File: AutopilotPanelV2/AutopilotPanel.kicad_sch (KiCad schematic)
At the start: 164 parts, among them J1 USB_C_Receptacle_USB2.0_16P, J10 PINHD_1x2_Male, J2 PINHD_1x2_Male, J3 PINHD_1x2_Male, J4 PINHD_1x2_Male, J5 PINHD_1x2_Male, J6 PINHD_1x2_Male, J7 PINHD_1x2_Male, J8 PINHD_1x2_Male, J9 PINHD_1x2_Male, Q1 NFET-SOT23, Q2 NFET-SOT23, Q3 NFET-SOT23, Q4 NFET-SOT23, Q5 NFET-SOT23, Q6 NFET-SOT23, SW1 SW_SPST_Tactile_6x6, SW10 SW_SPST_Tactile_6x6, SW11 SW_SPST_Tactile_6x6, SW12 SW_SPST_Tactile_6x6, SW13 SW_SPST_Tactile_6x6, SW14 SW_SPST_Tactile_6x6, SW15 RotaryEncoder_Switch_EC11E, SW2 SW_SPST_Tactile_6x6, SW3 SW_SPST_Tactile_6x6, SW4 SW_SPST_Tactile_6x6, SW5 SW_SPST_Tactile_6x6, SW6 SW_SPST_Tactile_6x6, SW7 SW_SPST_Tactile_6x6, SW8 SW_SPST_Tactile_6x6, SW9 SW_SPST_Tactile_6x6, U10 7SegmentFJ5161AH, U11 7SegmentFJ5161AH, U12 7SegmentFJ5161AH, U13 7SegmentFJ5161AH, U14 7SegmentFJ5161AH, U15 74HC165, U16 TPS62160DSG, U17 74HC165, U18 74HC595, U19 74HC595, U20 74HC595, U21 74HC595, U22 74HC595, U23 74HC595, U7 74HC164, U8 74HC164, U9 7SegmentFJ5161AH

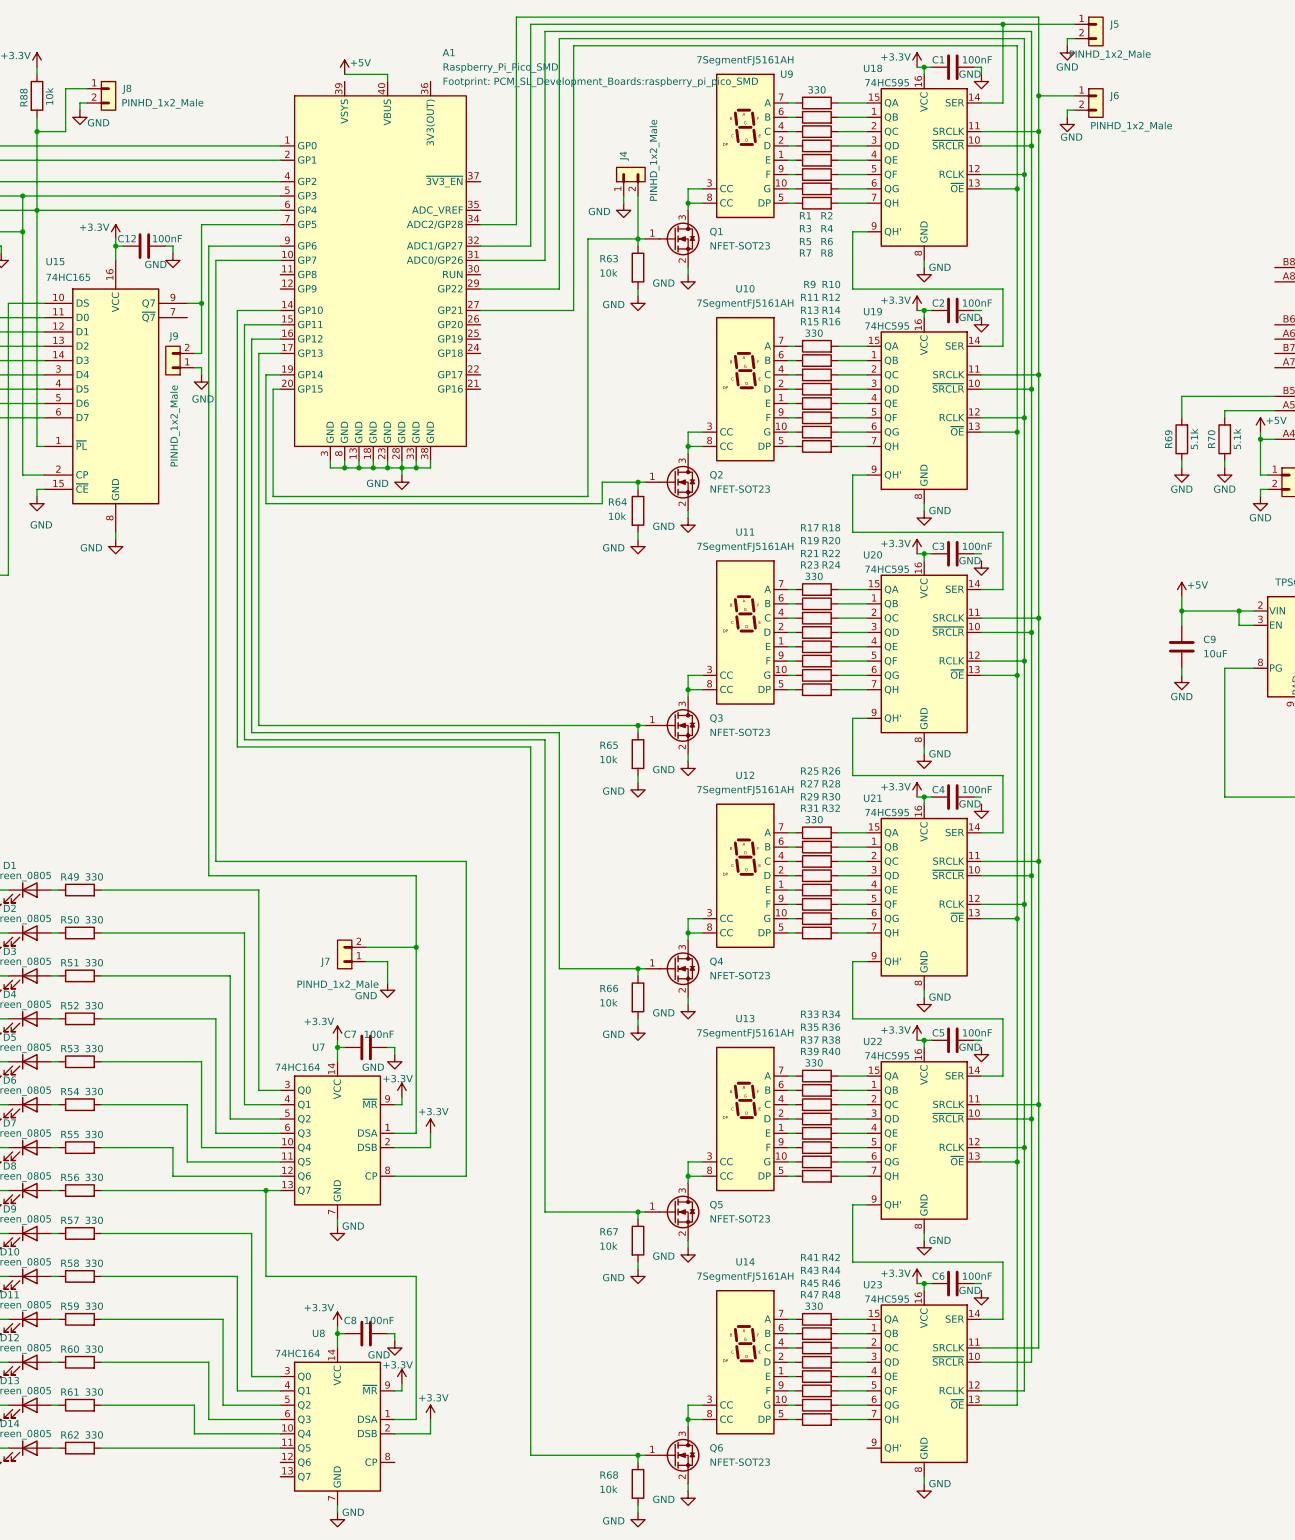
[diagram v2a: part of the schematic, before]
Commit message: Changed ButtonLED register from 74HC164 to 74HC595
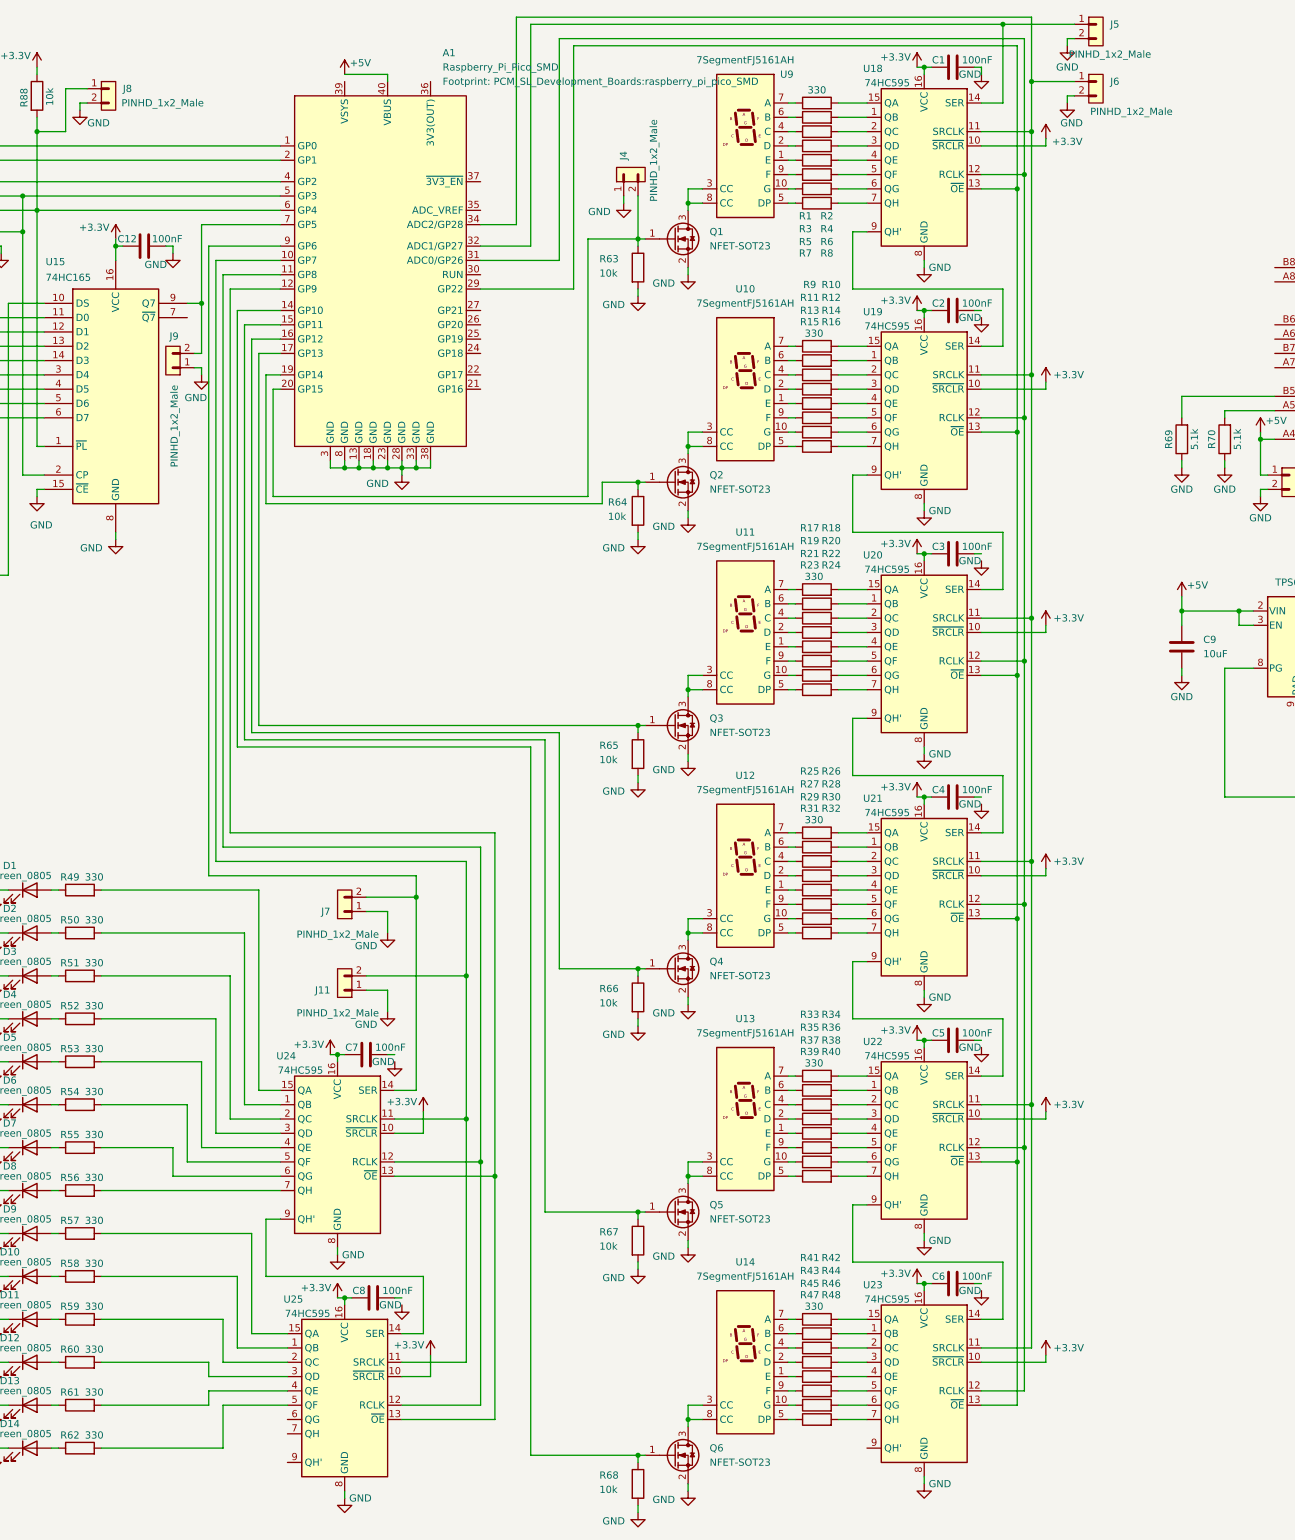
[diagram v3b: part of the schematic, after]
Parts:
- removed U7, U8: 74HC164, Package_SO:SOIC-14_3.9x8.7mm_P1.27mm, symbol 74xx:74HC164
- added J11: PINHD_1x2_Male, Connector_PinHeader_2.54mm:PinHeader_1x02_P2.54mm_Vertical, symbol PCM_SL_Pin_Headers:PINHD_1x2_Male
- added U24, U25: 74HC595, symbol 74xx:74HC595
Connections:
- net +3.3V: now also U18.10 (~{SRCLR}), U19.10 (~{SRCLR}), U20.10 (~{SRCLR}), U21.10 (~{SRCLR}), U22.10 (~{SRCLR}), U23.10 (~{SRCLR}), U24.10 (~{SRCLR}), U24.16 (VCC), U25.10 (~{SRCLR}), U25.16 (VCC)
- net GND: now also J11.1, U24.8 (GND), U25.8 (GND); no longer C7.2, C8.2
- net at R56.2: now also U24.7 (QH)
- net at R61.2: now also U25.4 (QE)
- net at R62.2: now also U25.5 (QF)
- net at R57.2: now also U25.15 (QA)
- net at R58.2: now also U25.1 (QB)
- net at R59.2: now also U25.2 (QC)
- net at R60.2: now also U25.3 (QD)
- net at U18.12 (RCLK), U19.12 (RCLK), U20.12 (RCLK)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: now also A1.31 (ADC0/GP26); no longer A1.29 (GP22)
- net at U18.13 (~{OE}), U19.13 (~{OE}), U20.13 (~{OE})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: now also A1.29 (GP22); no longer A1.27 (GP21)
- net at R53.2: now also U24.4 (QE)
- net at R52.2: now also U24.3 (QD)
- net at R55.2: now also U24.6 (QG)
- net at R54.2: now also U24.5 (QF)
- net at A1.10 (GP7): now also J11.2, U24.11 (SRCLK), U25.11 (SRCLK)
- net at A1.11 (GP8): now also U24.12 (RCLK), U25.12 (RCLK)
- net at A1.12 (GP9): now also U24.13 (~{OE}), U25.13 (~{OE})
- net at A1.9 (GP6), J7.2: now also U24.14 (SER)
- net at R49.2: now also U24.15 (QA)
- net at R50.2: now also U24.1 (QB)
- net at R51.2: now also U24.2 (QC)
- new net: U24.9 (QH'), U25.14 (SER)
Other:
- moved on the sheet: J6, J7
